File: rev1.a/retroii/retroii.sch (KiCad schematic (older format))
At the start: 0 parts

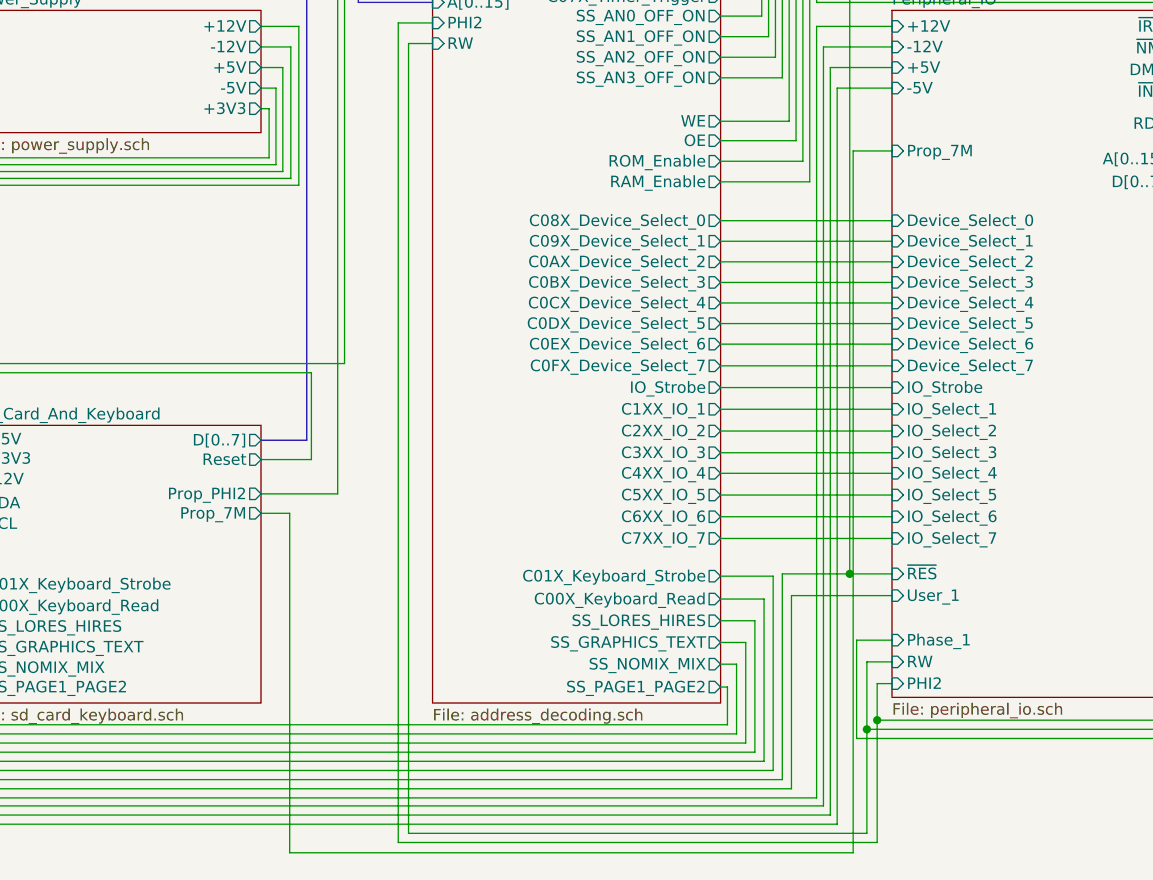
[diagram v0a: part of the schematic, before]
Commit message: added prop_q3 to peripheral slot connections.
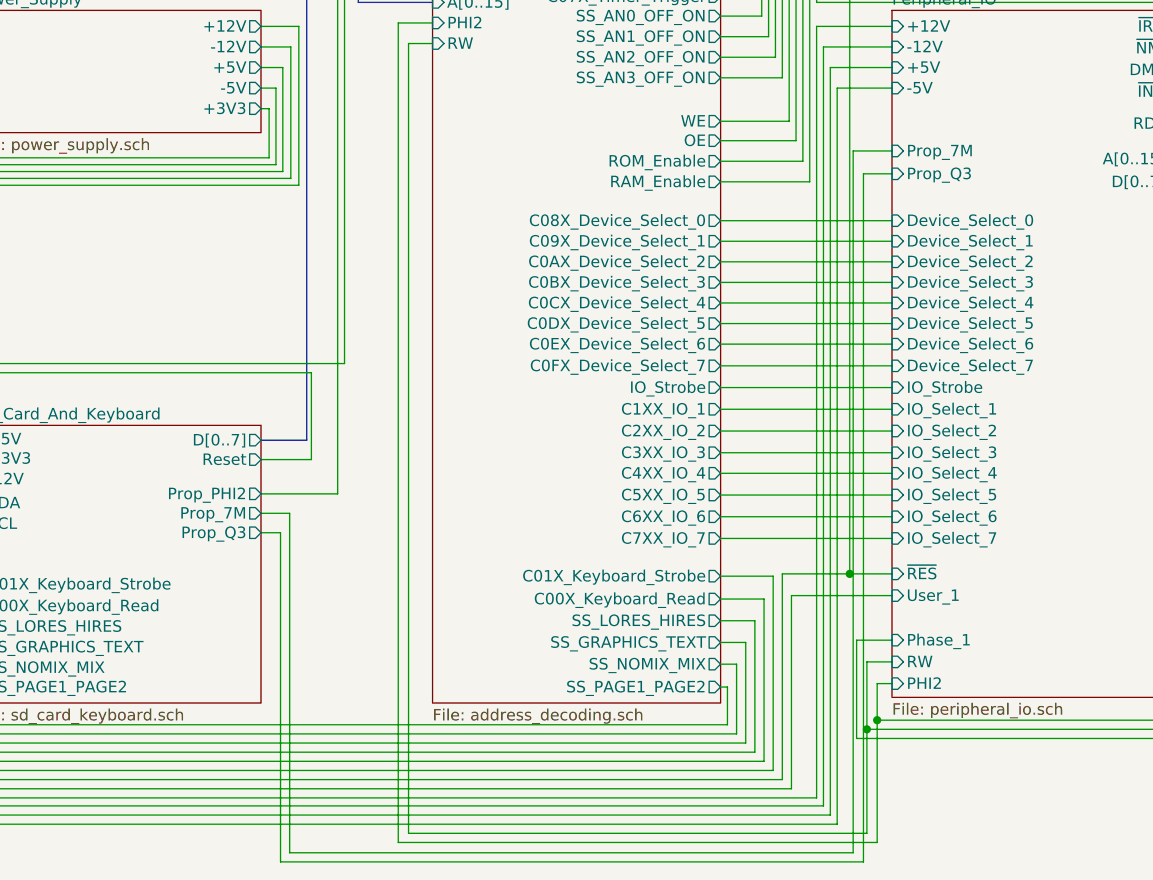
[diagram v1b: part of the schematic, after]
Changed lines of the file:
@@
 F15 "Prop_PHI2" O R 2705 6110 50
 F16 "Prop_7M" O R 2705 6195 50
+F17 "Prop_Q3" O R 2705 6280 50
 $EndSheet
 $Sheet
@@
 F33 "RDY" O R 6725 4490 50
 F34 "Prop_7M" I L 5465 4610 50
+F35 "Prop_Q3" I L 5465 4710 50
 $EndSheet
 Wire Wire Line
@@
 Wire Wire Line
 	4950 1510 5465 1510
+Wire Wire Line
+	2705 6280 2790 6280
+Wire Wire Line
+	2790 6280 2790 7720
+Wire Wire Line
+	2790 7720 5340 7720
+Wire Wire Line
+	5340 7720 5340 4710
+Wire Wire Line
+	5340 4710 5465 4710
 $EndSCHEMATC

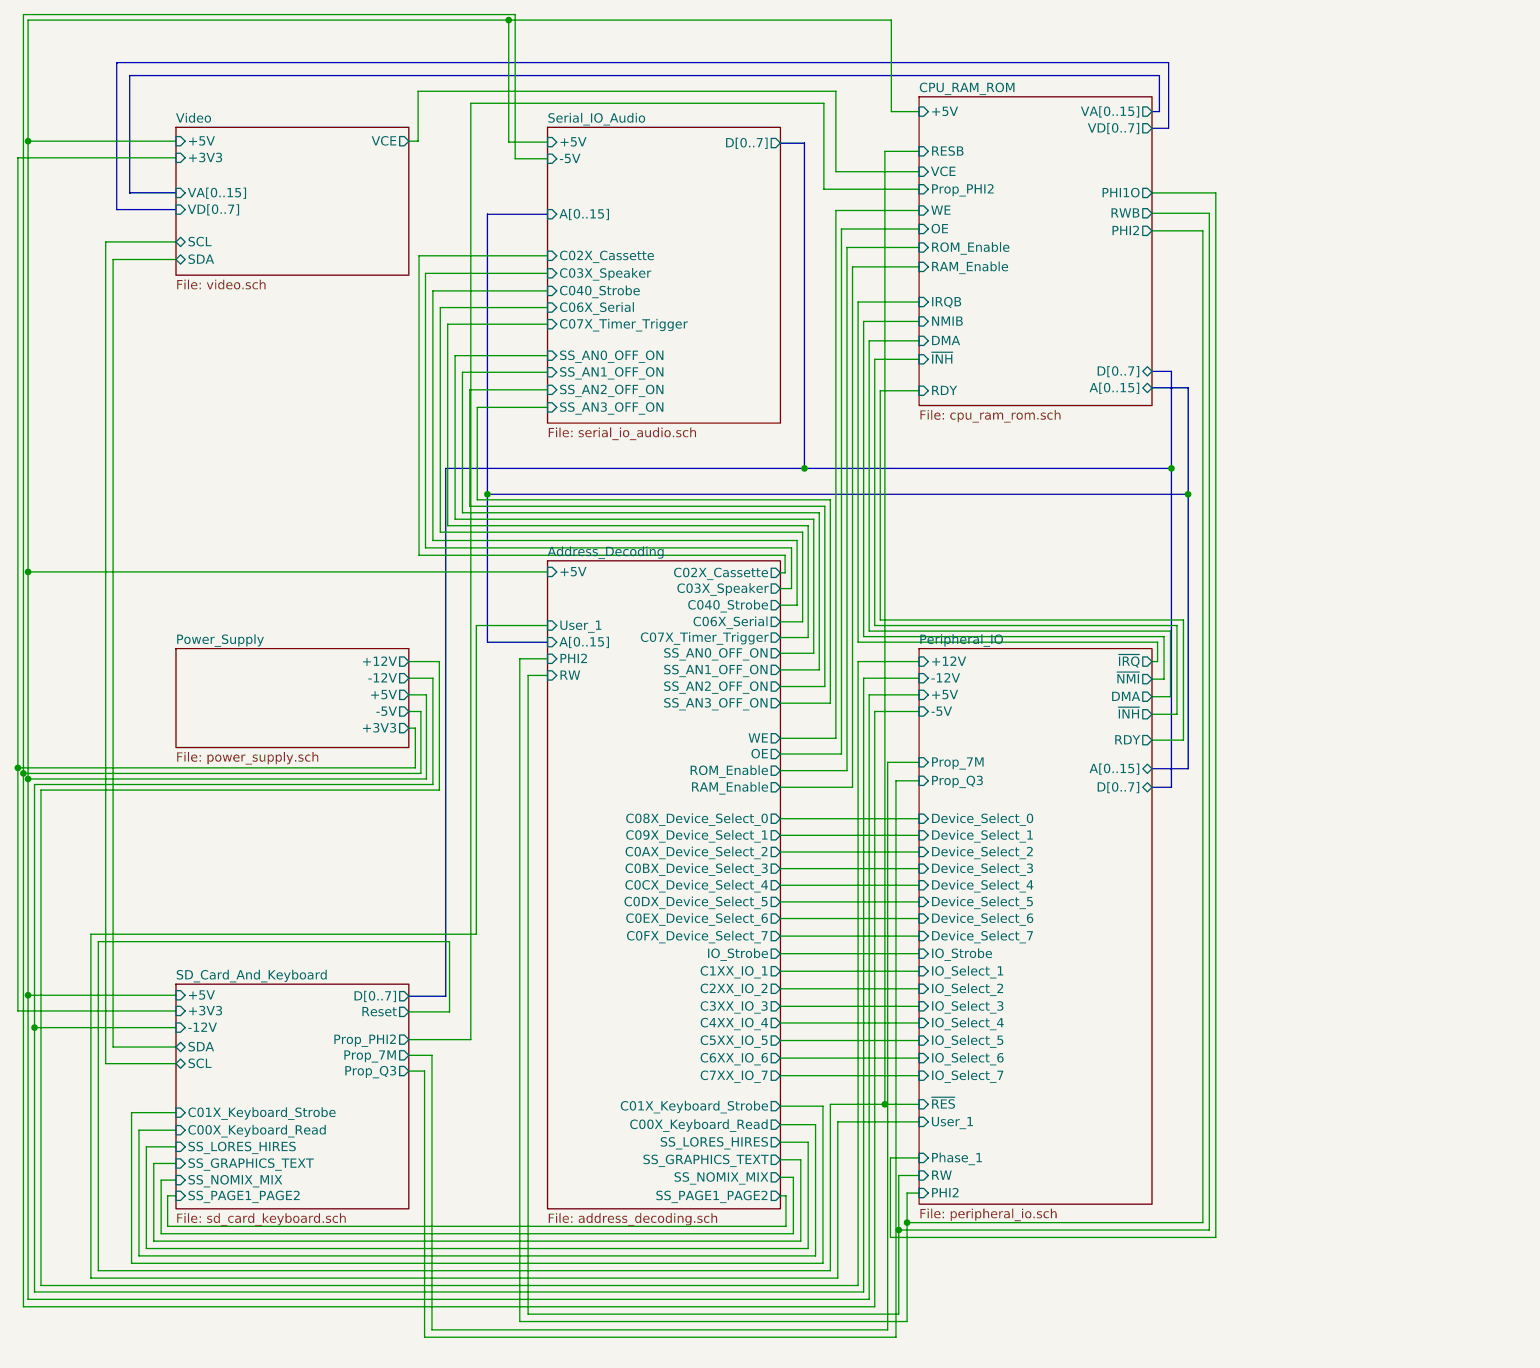
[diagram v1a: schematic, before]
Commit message: modified prop layout to include jumpers for phi2, rdy, and dma.
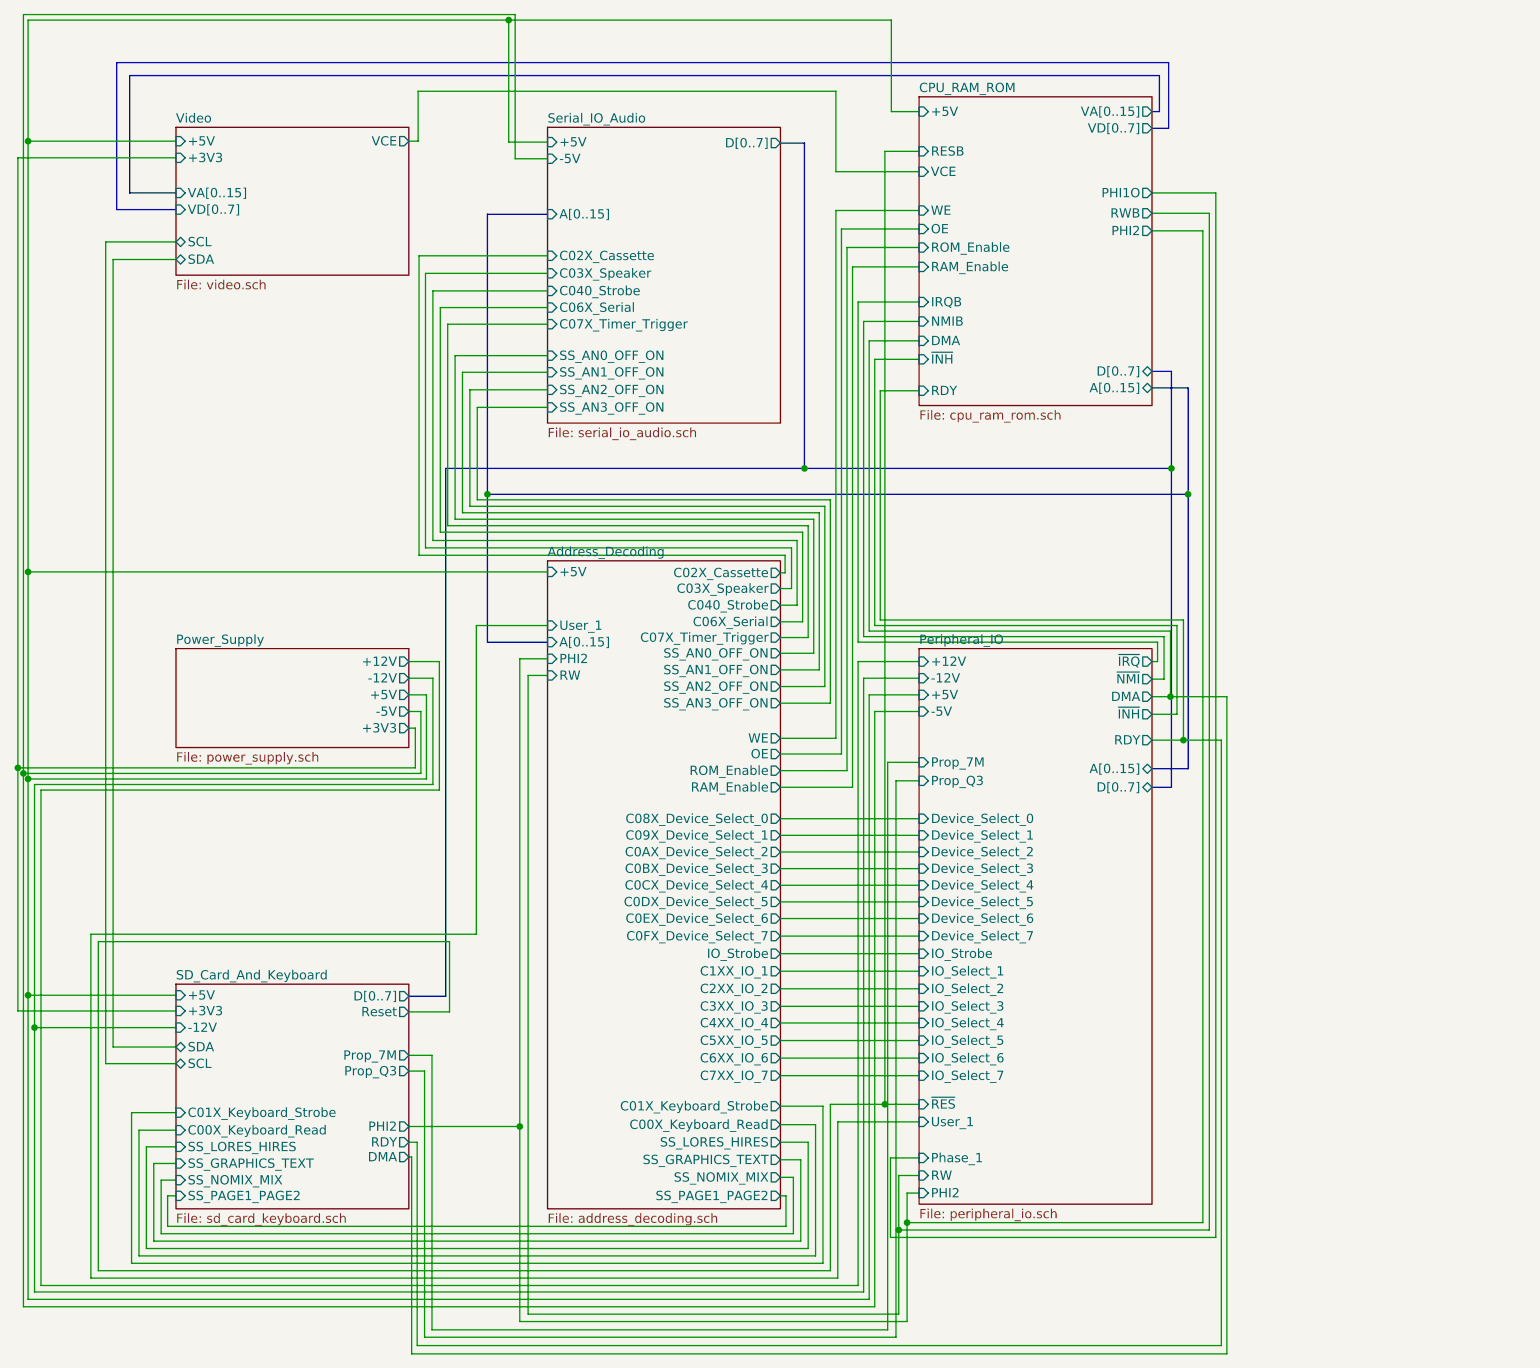
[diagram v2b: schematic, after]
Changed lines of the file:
@@
 F19 "D[0..7]" B R 6725 2495 50
 F20 "RDY" I L 5465 2600 50
-F21 "Prop_PHI2" I L 5465 1510 50
 $EndSheet
 $Sheet
@@
 F13 "D[0..7]" O R 2705 5875 50
 F14 "-12V" I L 1445 6045 50
-F15 "Prop_PHI2" O R 2705 6110 50
-F16 "Prop_7M" O R 2705 6195 50
-F17 "Prop_Q3" O R 2705 6280 50
+F15 "Prop_7M" O R 2705 6195 50
+F16 "Prop_Q3" O R 2705 6280 50
+F17 "PHI2" O R 2705 6580 50
+F18 "RDY" O R 2705 6665 50
+F19 "DMA" O R 2705 6745 50
 $EndSheet
 $Sheet
@@
 	3455 4050 3305 4050
 Wire Wire Line
-	3305 4050 3305 7635
+	3305 4050 3305 6580
 Wire Wire Line
 	3305 7635 5400 7635
@@
 	2830 6195 2705 6195
 Wire Wire Line
-	2705 6110 3040 6110
-Wire Wire Line
-	3040 6110 3040 1045
-Wire Wire Line
-	3040 1045 4950 1045
-Wire Wire Line
-	4950 1045 4950 1510
-Wire Wire Line
-	4950 1510 5465 1510
-Wire Wire Line
 	2705 6280 2790 6280
 Wire Wire Line
@@
 Wire Wire Line
 	5340 4710 5465 4710
+Wire Wire Line
+	2705 6580 3305 6580
+Connection ~ 3305 6580
+Wire Wire Line
+	3305 6580 3305 7635
+Wire Wire Line
+	2705 6665 2750 6665
+Wire Wire Line
+	2750 6665 2750 7765
+Wire Wire Line
+	2750 7765 7100 7765
+Wire Wire Line
+	7100 7765 7100 4490
+Wire Wire Line
+	7100 4490 6895 4490
+Connection ~ 6895 4490
+Wire Wire Line
+	6825 4255 7130 4255
+Wire Wire Line
+	7130 4255 7130 7810
+Wire Wire Line
+	7130 7810 2720 7810
+Wire Wire Line
+	2720 7810 2720 6745
+Wire Wire Line
+	2720 6745 2705 6745
+Connection ~ 6825 4255
 $EndSCHEMATC

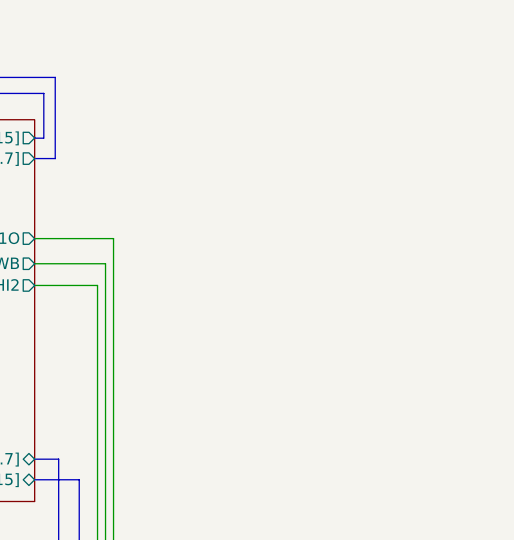
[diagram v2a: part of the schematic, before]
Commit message: added m4 mounting holes
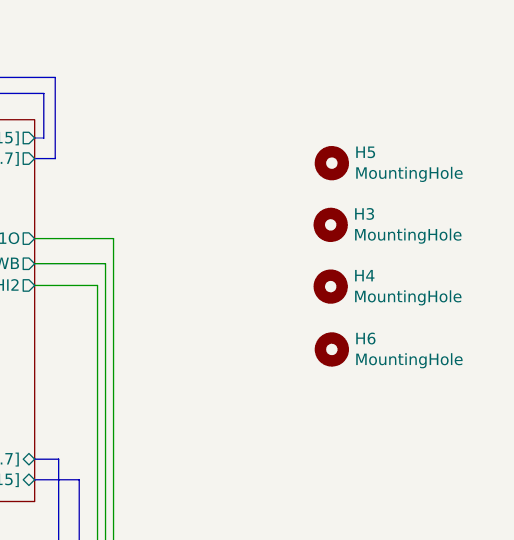
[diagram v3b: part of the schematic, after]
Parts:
- added H3, H4, H5, H6: MountingHole, MountingHole:MountingHole_4.3mm_M4_Pad_Via, symbol Mechanical:MountingHole
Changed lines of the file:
@@
 	2720 6745 2705 6745
 Connection ~ 6825 4255
+$Comp
+L Mechanical:MountingHole H5
+U 1 1 5D33552B
+P 8025 1200
+F 0 "H5" H 8125 1246 50  0000 L CNN
+F 1 "MountingHole" H 8125 1155 50  0000 L CNN
+F 2 "MountingHole:MountingHole_4.3mm_M4_Pad_Via" H 8025 1200 50  0001 C CNN
+F 3 "~" H 8025 1200 50  0001 C CNN
+	1    8025 1200
+	1    0    0    -1
+$EndComp
+$Comp
+L Mechanical:MountingHole H3
+U 1 1 5D335991
+P 8020 1470
+F 0 "H3" H 8120 1516 50  0000 L CNN
+F 1 "MountingHole" H 8120 1425 50  0000 L CNN
+F 2 "MountingHole:MountingHole_4.3mm_M4_Pad_Via" H 8020 1470 50  0001 C CNN
+F 3 "~" H 8020 1470 50  0001 C CNN
+	1    8020 1470
+	1    0    0    -1
+$EndComp
+$Comp
+L Mechanical:MountingHole H4
+U 1 1 5D335BAF
+P 8020 1740
+F 0 "H4" H 8120 1786 50  0000 L CNN
+F 1 "MountingHole" H 8120 1695 50  0000 L CNN
+F 2 "MountingHole:MountingHole_4.3mm_M4_Pad_Via" H 8020 1740 50  0001 C CNN
+F 3 "~" H 8020 1740 50  0001 C CNN
+	1    8020 1740
+	1    0    0    -1
+$EndComp
+$Comp
+L Mechanical:MountingHole H6
+U 1 1 5D335CD5
+P 8025 2015
+F 0 "H6" H 8125 2061 50  0000 L CNN
+F 1 "MountingHole" H 8125 1970 50  0000 L CNN
+F 2 "MountingHole:MountingHole_4.3mm_M4_Pad_Via" H 8025 2015 50  0001 C CNN
+F 3 "~" H 8025 2015 50  0001 C CNN
+	1    8025 2015
+	1    0    0    -1
+$EndComp
 $EndSCHEMATC
